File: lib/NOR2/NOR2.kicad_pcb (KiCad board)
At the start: 2 copper layers, 4 parts

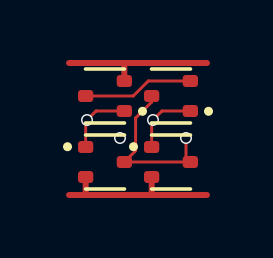
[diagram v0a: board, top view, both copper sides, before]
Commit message: All cells now use 1mm*4mm grid rather than 1.1mm*4.4mm
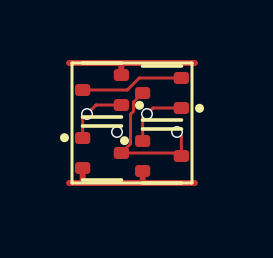
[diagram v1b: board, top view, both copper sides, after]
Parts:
- moved N2 0.36 mm to (3.00, 3.10)
- moved N1 0.32 mm to (1.00, 3.00)
- moved P2 0.32 mm to (3.00, 1.00)
- moved P1 0.22 mm to (1.00, 0.90)
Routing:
- net GND: track 5.80 -> 5.15 mm
- net VDD: track 5.19 -> 4.63 mm

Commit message: Make the pads of my SOT523 footprint very slightly smaller, which is enough to route all the cells and leave the mosfets exactly on the grid
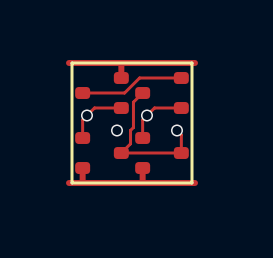
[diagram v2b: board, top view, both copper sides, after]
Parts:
- N1, N2, P1, P2: footprint Package_TO_SOT_SMD:SOT-523 -> RV523:SOT523
- moved N2 0.10 mm to (3.00, 3.00)
- moved P1 0.10 mm to (1.00, 1.00)

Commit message: Propagate MOSFET values to the cells' PCBs
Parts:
- N1, N2: value (none) -> NMOS
- P1, P2: value (none) -> PMOS
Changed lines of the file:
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@@
 			)
 		)
-		(property "Value" ""
+		(property "Value" "PMOS"
 			(at 0 0 180)
 			(layer "F.Fab")
@@
 			)
 		)
-		(property "Value" ""
+		(property "Value" "NMOS"
 			(at 0 0 0)
 			(layer "F.Fab")
@@
 			)
 		)
-		(property "Value" ""
+		(property "Value" "PMOS"
 			(at 0 0 180)
 			(layer "F.Fab")
@@
 			)
 		)
-		(property "Value" ""
+		(property "Value" "NMOS"
 			(at 0 0 0)
 			(layer "F.Fab")
